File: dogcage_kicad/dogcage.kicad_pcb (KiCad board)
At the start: 2 copper layers, 0 parts

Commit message: Fixed diode orientation and layout WIP
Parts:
- added C1: 10uF, Capacitors_Elko_ThroughHole:Elko_vert_11x5mm_RM2, F.Cu at (125.7, 96.5)
- added C2: 10uF, Capacitors_Elko_ThroughHole:Elko_vert_20x10mm_RM5, F.Cu at (142.2, 91.4)
- added CON1: BARREL_JACK, Connect:BARREL_JACK, F.Cu at (100.3, 78.7)
- added D1: Assoc LED, LEDs:LED-3MM, F.Cu at (193.0, 114.3)
- added D2: 1N4001, Diodes_ThroughHole:Diode_DO-41_SOD81_Horizontal_RM10, F.Cu at (124.5, 78.7)
- added M1: XBEE, modules:xbee, F.Cu at (167.6, 88.9)
- added P1: Door Sensor, Pin_Headers:Pin_Header_Straight_1x02, F.Cu at (177.8, 152.4)
- added P2: Servo, Pin_Headers:Pin_Header_Straight_1x03, F.Cu at (172.7, 139.7)
- added P3: CONN_01X10, Pin_Headers:Pin_Header_Straight_1x10, F.Cu at (149.9, 78.7)
- added P4: CONN_01X10, Pin_Headers:Pin_Header_Straight_1x10, F.Cu at (185.4, 80.0)
- added P5: CONN_01X14, Pin_Headers:Pin_Header_Straight_1x14, F.Cu at (96.5, 114.3)
- added P6: CONN_01X05, Pin_Headers:Pin_Header_Straight_1x05, F.Cu at (115.6, 153.7)
- added P7: CONN_01X14, Pin_Headers:Pin_Header_Straight_1x14, F.Cu at (124.5, 114.3)
- added Q1: TIP120, Power_Integrations:TO-220, F.Cu at (137.2, 151.1)
- added R1: 330, Resistors_ThroughHole:Resistor_Horizontal_RM20mm, F.Cu at (193.0, 97.8)
- added SW1: SW_PUSH, Buttons_Switches_ThroughHole:SW_PUSH_SMALL, F.Cu at (157.5, 153.7)
- added U1: LD1117S33TR, SMD_Packages:SOT-223, F.Cu at (135.9, 82.5)
- added U2: TEENSYLC, modules:Teensy-3.1, F.Cu at (102.9, 116.8)
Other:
- board outline added: 102.9 x 85.1 mm

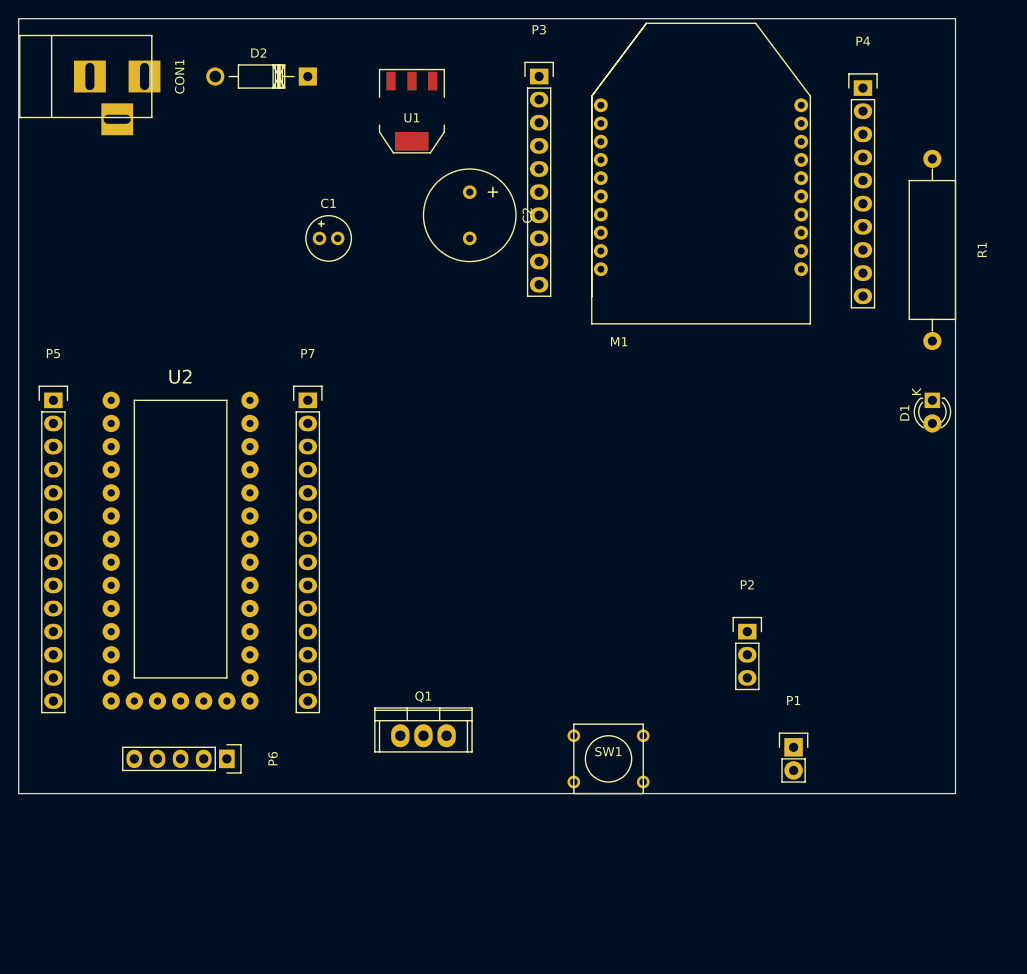
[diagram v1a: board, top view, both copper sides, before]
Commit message: Fixed cap and resistor footprints, improved overall placement
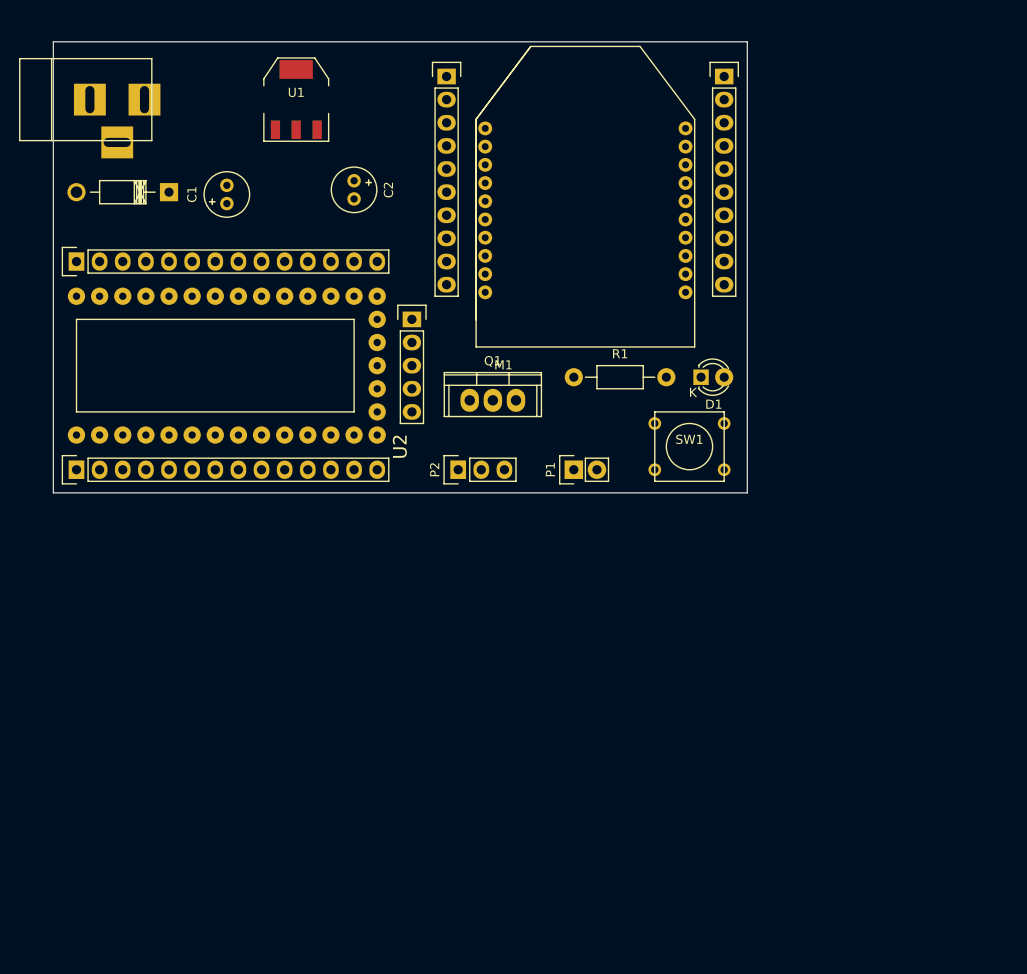
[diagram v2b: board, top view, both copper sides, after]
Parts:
- C2: footprint Capacitors_Elko_ThroughHole:Elko_vert_20x10mm_RM5 -> Capacitors_Elko_ThroughHole:Elko_vert_11x5mm_RM2
- R1: footprint Resistors_ThroughHole:Resistor_Horizontal_RM20mm -> Resistors_ThroughHole:Resistor_Horizontal_RM10mm
- moved P6 52.4 mm to (135.9, 105.4), turned to 0 degrees
- moved P1 38.9 mm to (153.7, 121.9), turned to 90 degrees
- moved Q1 37.6 mm to (144.8, 114.3)
- moved R1 37.0 mm to (158.8, 111.8), turned to 0 degrees
- moved P2 36.4 mm to (141.0, 121.9), turned to 90 degrees
- moved SW1 35.4 mm to (166.4, 119.4)
- moved P7 29.6 mm to (99.1, 99.1), turned to 90 degrees
- moved D1 25.5 mm to (167.6, 111.8), turned to 0 degrees
- moved D2 19.8 mm to (109.2, 91.4)
- moved P4 15.3 mm to (170.2, 78.7)
- moved M1 13.0 mm to (154.9, 91.4)
- moved C2 12.8 mm to (129.5, 90.2)
- moved U1 12.8 mm to (123.2, 81.3), turned to 0 degrees
- moved C1 10.9 mm to (115.6, 92.7), turned to 90 degrees
- moved P3 10.2 mm to (139.7, 78.7)
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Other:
- board size 102.9 x 85.1 mm -> 76.2 x 49.5 mm

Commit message: Layout checkpoint
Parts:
- moved SW1 46.8 mm to (130.8, 88.9), turned to 180 degrees
- moved R1 11.7 mm to (170.2, 114.3), turned to 270 degrees
- moved C2 11.7 mm to (121.9, 81.3), turned to 90 degrees
- moved C1 11.5 mm to (114.8, 81.3)
- moved U1 11.4 mm to (118.1, 91.4), turned to 180 degrees
- moved D1 9.67 mm to (163.8, 120.7)
- moved P3 3.05 mm to (139.7, 81.8)
- moved P4 3.05 mm to (170.2, 81.8)
- moved P1 2.54 mm to (151.1, 121.9)
- moved P2 1.27 mm to (139.7, 121.9)
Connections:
- D1 pad 1: Net-(D1-Pad1) -> GND
- D1 pad 2: GND -> Net-(D1-Pad2)
- M1 pad 12: /XBEE_DIO7 -> Net-(M1-Pad12)
- M1 pad 9: Net-(M1-Pad9) -> /XBEE_CTL
- P3 pad 9: Net-(M1-Pad9) -> /XBEE_CTL
- P4 pad 9: /XBEE_DIO7 -> Net-(M1-Pad12)
- P5 pad 8: /XBEE_DIO7 -> Net-(P5-Pad8)
- P7 pad 14: Net-(P7-Pad14) -> /XBEE_CTL
- R1 pad 2: Net-(D1-Pad1) -> Net-(D1-Pad2)
- U2 pad 20: Net-(P7-Pad14) -> /XBEE_CTL
- U2 pad 8: /XBEE_DIO7 -> Net-(P5-Pad8)
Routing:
- net GND: track 0.00 -> 40.1 mm, vias 0 -> 3
- net +5V: track 0.00 -> 32.4 mm
- net +3V3: track 0.00 -> 31.8 mm
- net Net-(CON1-Pad1): track 0.00 -> 23.0 mm
- net /XBEE_CTL: track 0.00 -> 16.7 mm
- net Net-(P2-Pad1): track 0.00 -> 11.7 mm
- net Net-(P7-Pad12): track 0.00 -> 11.4 mm
- net Net-(P1-Pad1): track 0.00 -> 8.67 mm, vias 0 -> 1
- net Net-(P2-Pad3): track 0.00 -> 7.62 mm
- net Net-(M1-Pad20): track 0.00 -> 5.34 mm
- net Net-(M1-Pad11): track 0.00 -> 5.15 mm
- net Net-(M1-Pad19): track 0.00 -> 5.11 mm
- net Net-(M1-Pad2): track 0.00 -> 5.11 mm
- net Net-(M1-Pad12): track 0.00 -> 4.93 mm
- net Net-(M1-Pad3): track 0.00 -> 4.89 mm
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- added copper zone on B.Cu, net GND

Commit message: Routing complete
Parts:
- removed P6: CONN_01X05, Pin_Headers:Pin_Header_Straight_1x05
- CON1: value BARREL_JACK -> 5V
- D1: value Assoc LED -> Assoc
- P1: value Door Sensor -> Door
- moved CON1 129.0 mm to (193.8, 170.2), turned to 180 degrees
- moved C1 106.2 mm to (168.9, 172.7)
- moved U1 99.6 mm to (179.1, 170.2), turned to 270 degrees
- moved D2 97.9 mm to (176.5, 162.6), turned to 0 degrees
- moved C2 96.1 mm to (168.9, 165.1)
- moved SW1 81.4 mm to (134.6, 170.2), turned to 0 degrees
- moved P7 63.7 mm to (154.9, 129.5), turned to 0 degrees
- moved Q1 57.1 mm to (161.3, 168.9), turned to 270 degrees
- moved M1 56.8 mm to (180.3, 142.2)
- moved P3 56.3 mm to (165.1, 132.1)
- moved P4 56.3 mm to (195.6, 132.1)
- moved P1 48.7 mm to (144.8, 170.2), turned to 0 degrees
- moved P2 47.1 mm to (151.1, 167.6), turned to 0 degrees
- moved D1 39.6 mm to (160.0, 160.0), turned to 90 degrees
- moved U2 37.0 mm to (135.9, 132.1), turned to 270 degrees
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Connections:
- M1 pad 4: Net-(M1-Pad4) -> /XBEE_CTL
- M1 pad 9: /XBEE_CTL -> Net-(M1-Pad9)
- P3 pad 4: Net-(M1-Pad4) -> /XBEE_CTL
- P3 pad 9: /XBEE_CTL -> Net-(M1-Pad9)
- P5 pad 12: Net-(P1-Pad1) -> Net-(P5-Pad12)
- P5 pad 14: Net-(P5-Pad14) -> Net-(P1-Pad1)
- P7 pad 14: /XBEE_CTL -> Net-(P7-Pad14)
- P7 pad 4: Net-(P7-Pad4) -> /XBEE_CTL
- Q1 pad 1: Net-(P5-Pad14) -> Net-(Q1-Pad1)
- SW1 pad 1: Net-(P7-Pad12) -> Net-(P5-Pad13)
- U2 pad 12: Net-(P1-Pad1) -> Net-(P5-Pad12)
- U2 pad 14: Net-(P5-Pad14) -> Net-(P1-Pad1)
- U2 pad 19: Net-(P6-Pad1) -> Net-(Q1-Pad1)
- U2 pad 20: /XBEE_CTL -> Net-(P7-Pad14)
- U2 pad 30: Net-(P7-Pad4) -> /XBEE_CTL
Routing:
- net Net-(M1-Pad15): track 4.26 -> 67.3 mm, vias 0 -> 2
- net +5V: track 32.4 -> 93.8 mm, vias 0 -> 4
- net GND: track 40.1 -> 63.2 mm, vias 3 -> 6
- net Net-(P5-Pad13): track 3.81 -> 21.5 mm
- net +3V3: track 31.8 -> 47.9 mm, vias 0 -> 1
- net Net-(CON1-Pad1): track 23.0 -> 8.23 mm
- net Net-(Q1-Pad1): track 0.00 -> 14.3 mm
- net Net-(P1-Pad1): track 8.67 -> 16.6 mm, vias 1 -> 0
- net Net-(P7-Pad12): track 11.4 -> 3.81 mm
- net Net-(D1-Pad2): track 0.00 -> 5.08 mm
- net Net-(M1-Pad9): track 0.00 -> 4.72 mm
- net Net-(M1-Pad4): track 4.67 -> 0.00 mm
- net Net-(P2-Pad3): track 7.62 -> 11.7 mm
- net Net-(P7-Pad4): track 3.81 -> 0.00 mm
- net Net-(P7-Pad14): track 0.00 -> 3.81 mm
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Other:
- board size 76.2 x 49.5 mm -> 68.6 x 49.8 mm

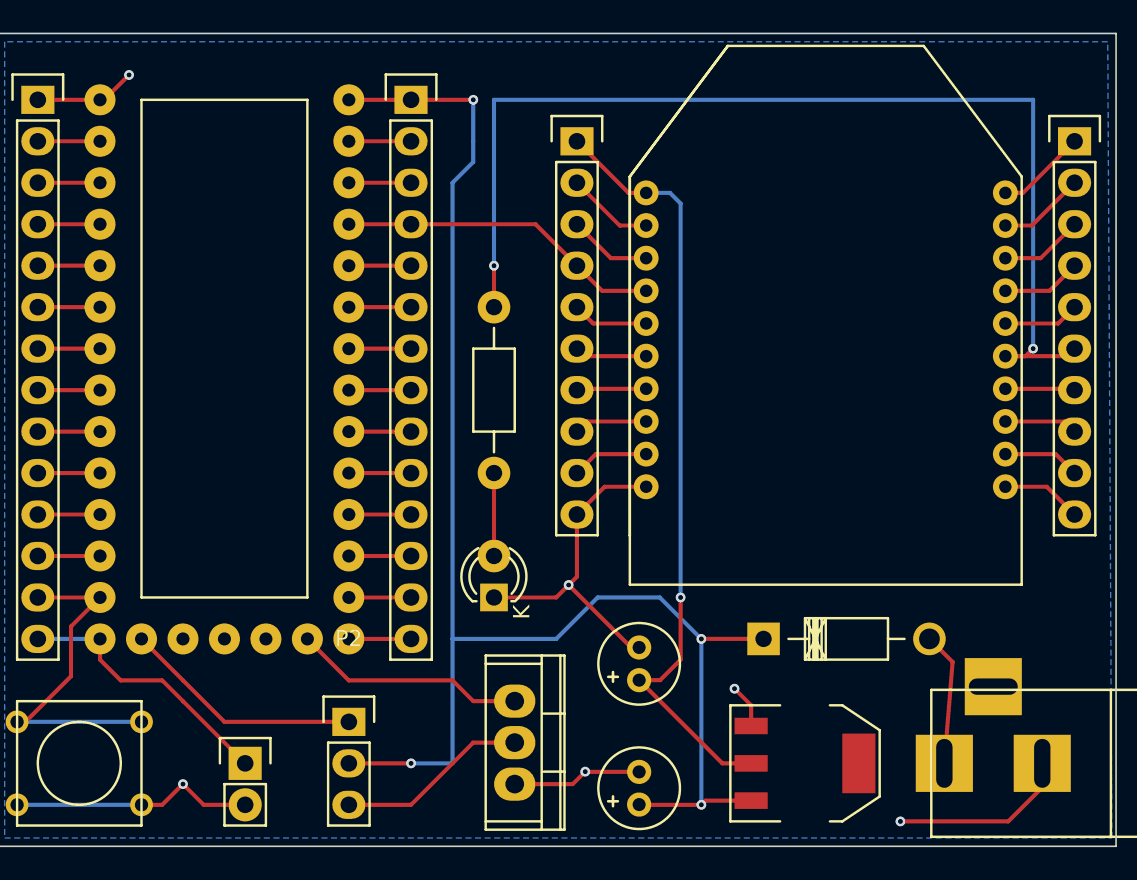
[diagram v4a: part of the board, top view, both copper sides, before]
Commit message: Updated design rules for oshpark, getting drc failures on vias
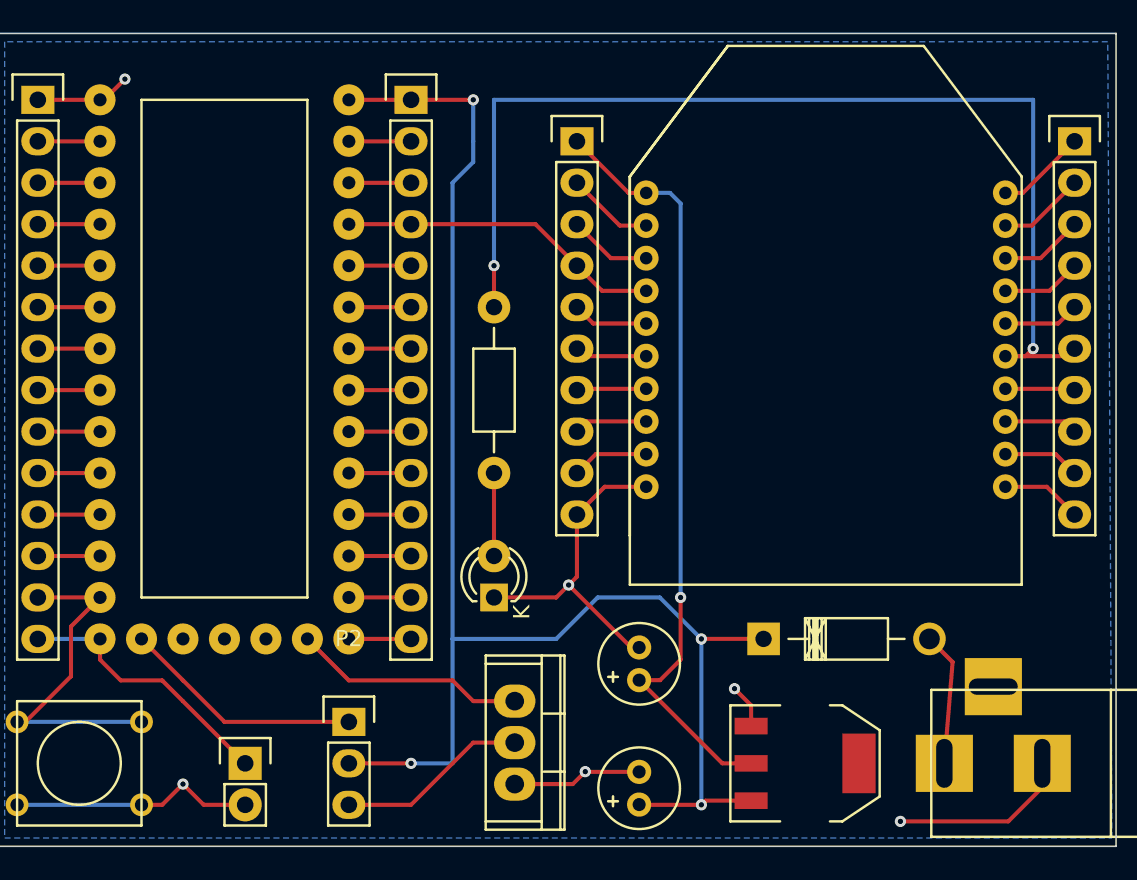
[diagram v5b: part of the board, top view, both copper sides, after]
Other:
- net class Default: trace_width 0.25 -> 0.254; via_dia 0.6 -> 0.6858; via_drill 0.4 -> 0.3302
- rule trace_min: 0.2 -> 0.1524
- rule via_min_drill: 0.3 -> 0.3302
- rule via_min_size: 0.4 -> 0.6858

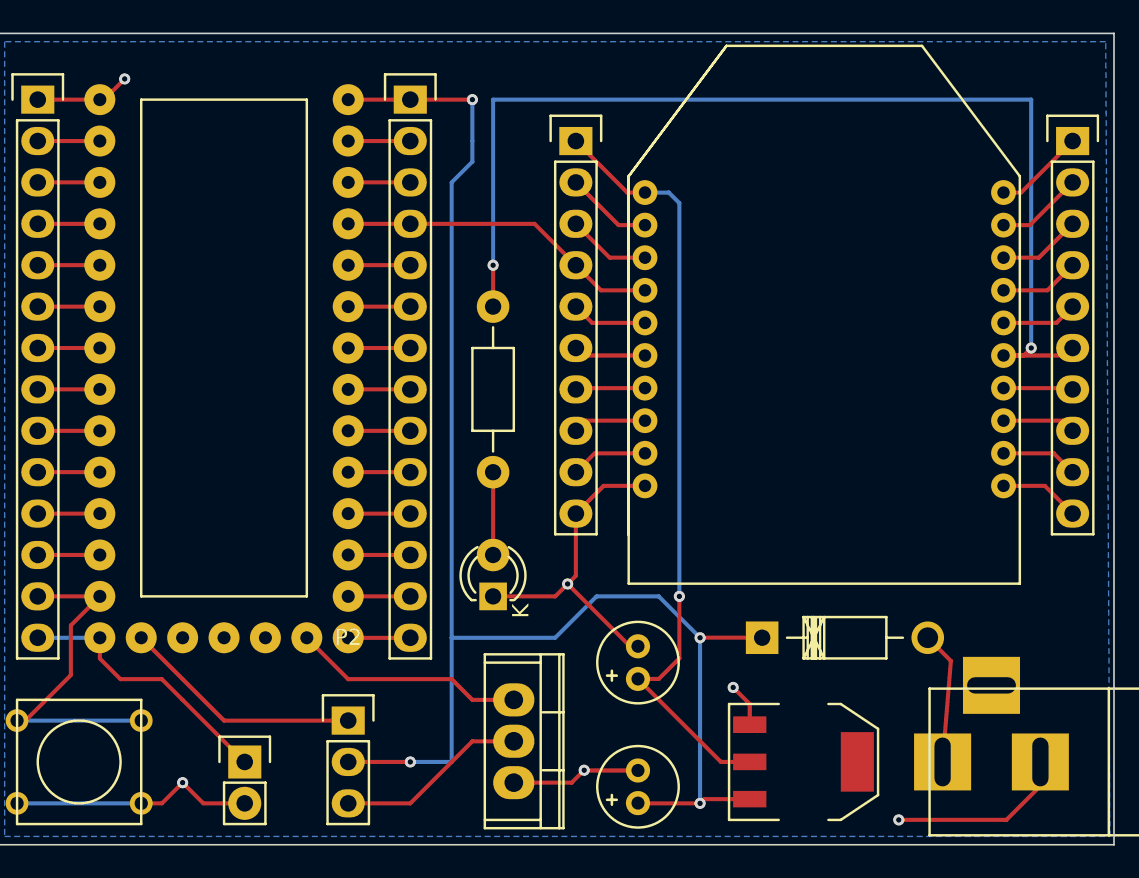
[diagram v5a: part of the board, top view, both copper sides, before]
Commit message: Fixed drc failure, moved trace out of keep-out zone
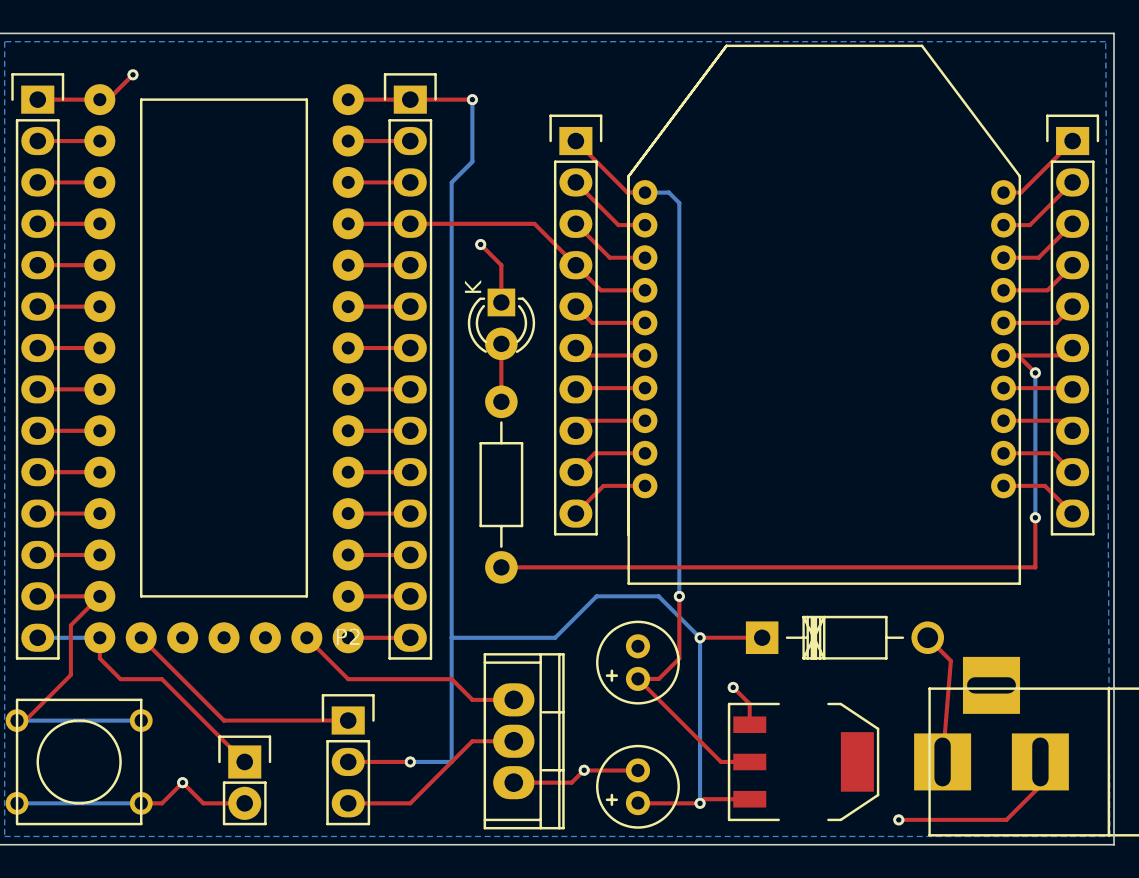
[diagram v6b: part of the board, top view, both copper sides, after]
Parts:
- moved D1 18.0 mm to (160.5, 142.0), turned to 270 degrees
- moved R1 5.86 mm to (160.5, 153.2), turned to 90 degrees
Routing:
- net Net-(M1-Pad15): track 67.3 -> 51.5 mm
- net GND: track 62.8 -> 53.7 mm
- net Net-(D1-Pad2): track 5.08 -> 3.56 mm
